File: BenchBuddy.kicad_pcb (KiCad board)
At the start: 4 copper layers, 165.1 x 63.5 mm, 125 parts, among them K1 1461069-5, P1 24 Pin MiniFit JR, P2 CONN_3X2, P3 CONN_2, P4 12 Pin Terminal Block, P5 3 Pin TB, Q1 2N3904, Q2 DMN65D8L-7, Q3 AOD476, Q4 AOD476, SW1 Power Switch, U1 LTV-816S, U11 LM317, U2 MCP3901, U3 LMT84, U4 OPA4170, U5 MCP4801, U6 LM337T, U7 AP5726, U8 LM337T, U9 LM317

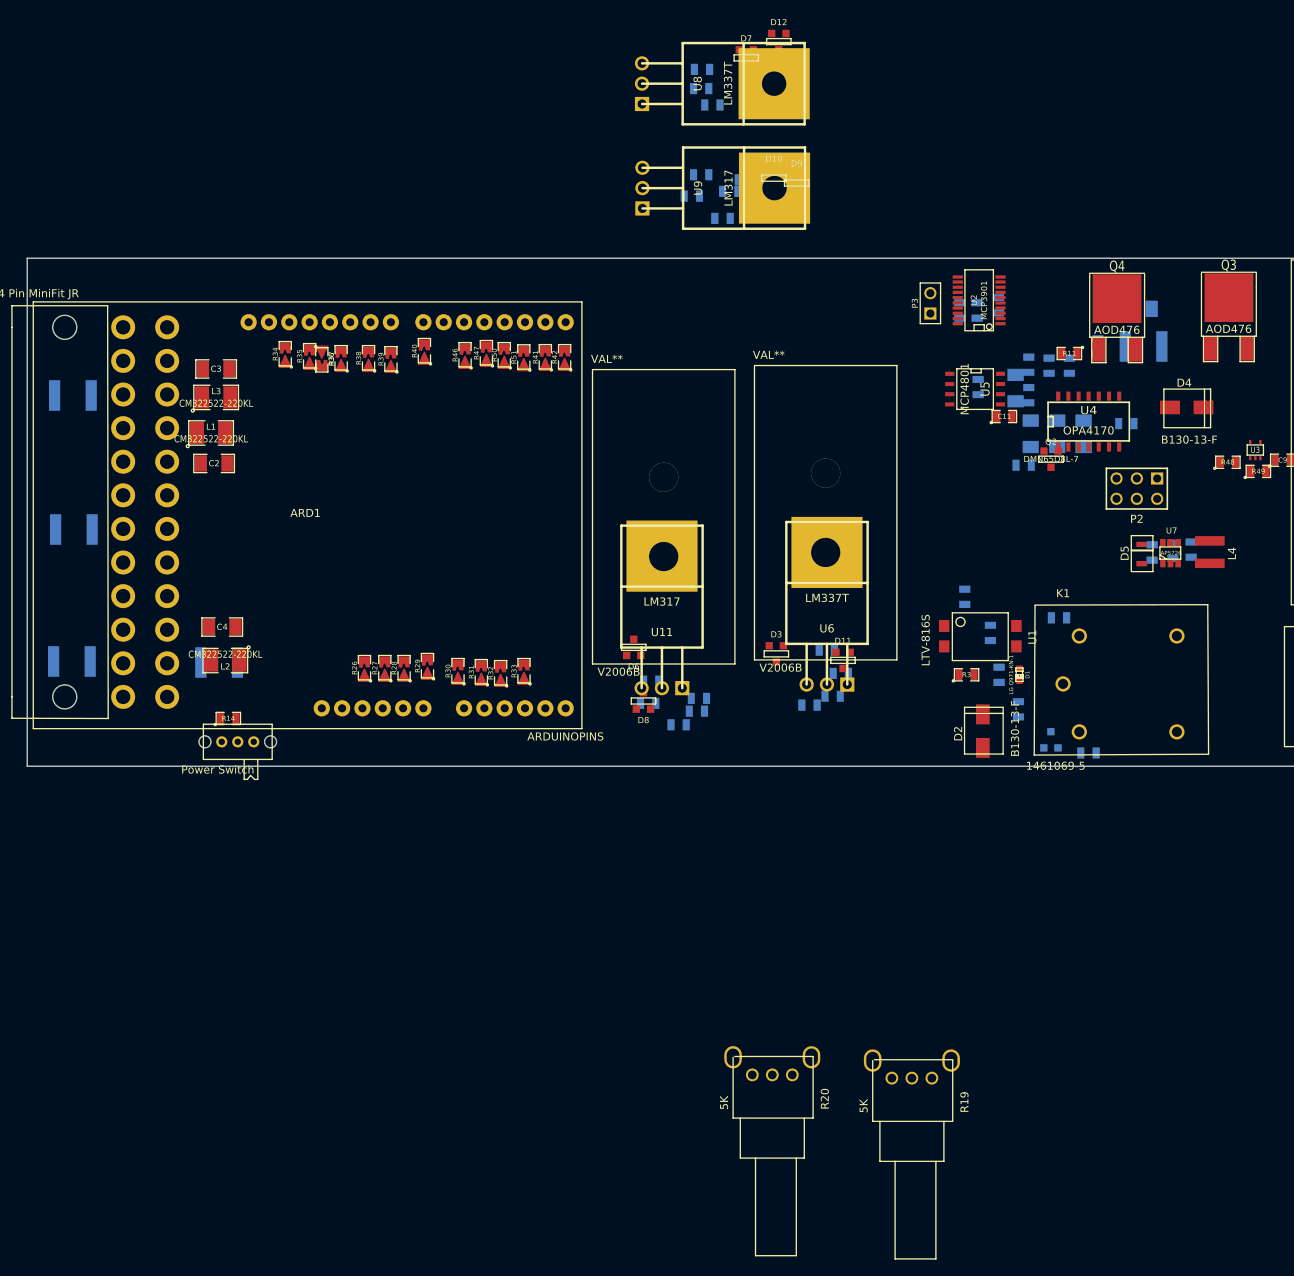
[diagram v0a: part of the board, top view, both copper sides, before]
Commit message: Added more ground planes
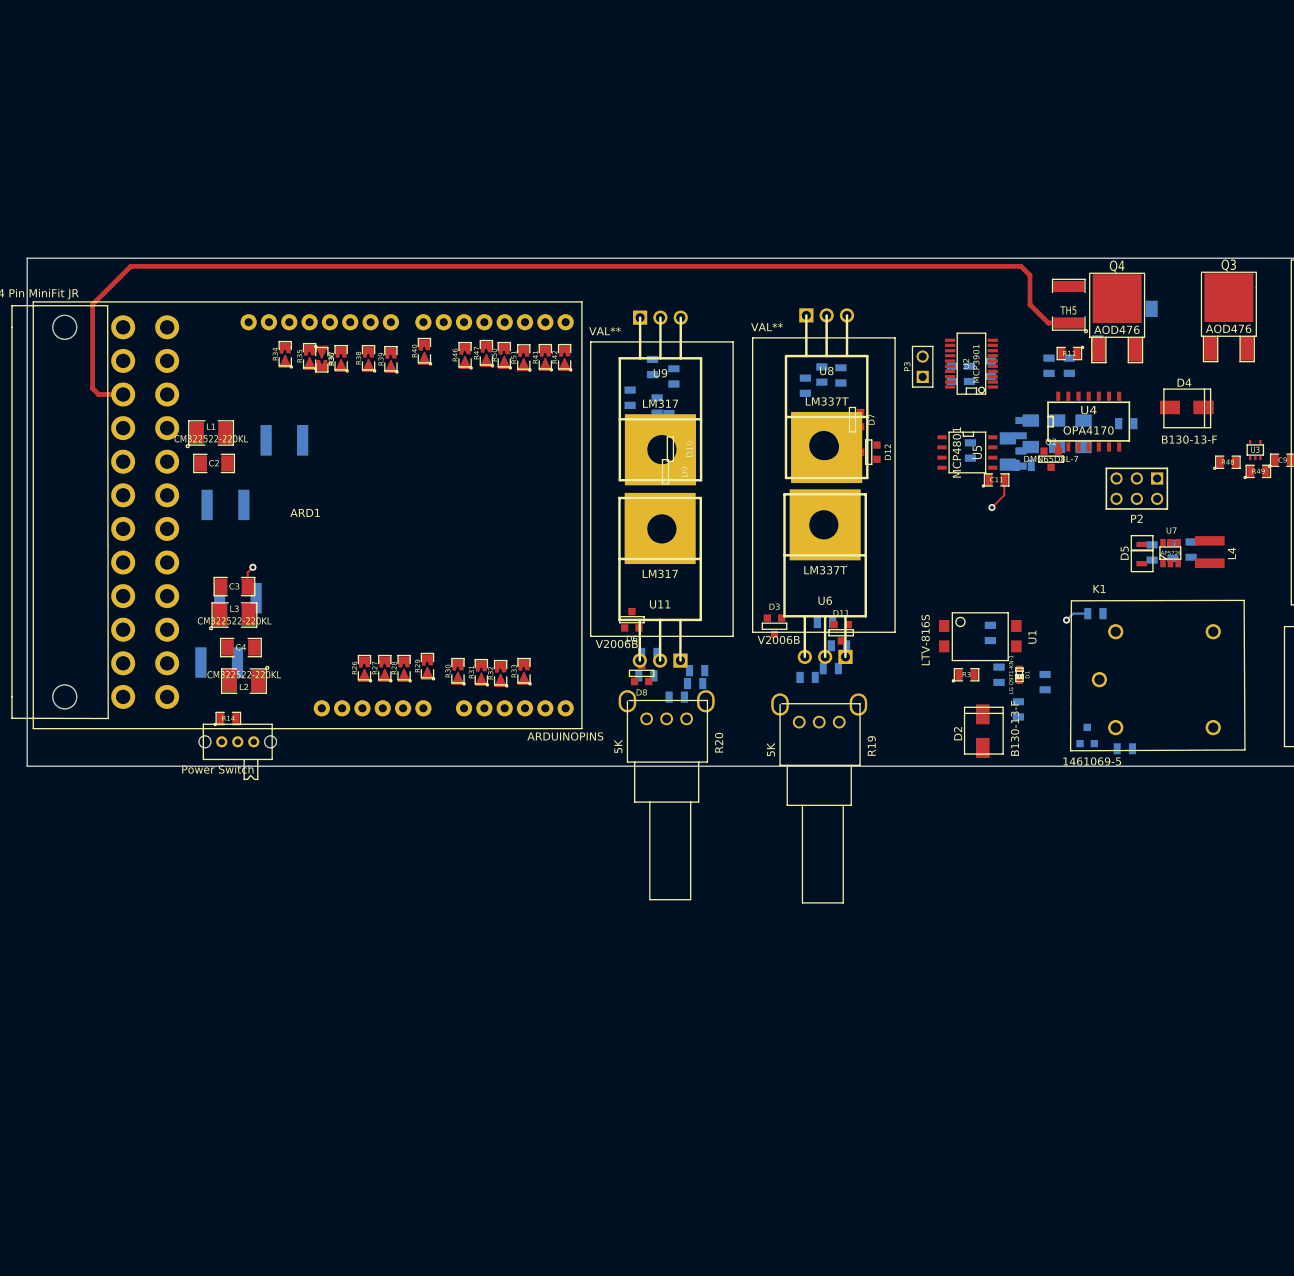
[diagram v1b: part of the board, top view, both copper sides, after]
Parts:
- TH5: moved to F.Cu
- moved D12 52.5 mm to (241.5, 120.0), turned to 270 degrees
- moved C23 50.9 mm to (238.6, 122.0), turned to 90 degrees
- moved C25 48.7 mm to (236.3, 122.3), turned to 270 degrees
- moved D7 47.1 mm to (239.4, 115.9), turned to 270 degrees
- moved R20 46.4 mm to (216.2, 153.3)
- moved R19 46.0 mm to (235.3, 153.7)
- moved R24 45.9 mm to (233.8, 122.2), turned to 270 degrees
- moved R53 42.0 mm to (238.0, 110.4), turned to 270 degrees
- moved C21 40.9 mm to (233.9, 116.4), turned to 270 degrees
- moved D9 39.7 mm to (216.1, 122.5), turned to 270 degrees
- moved C15 38.8 mm to (235.6, 110.3), turned to 270 degrees
- moved U8 37.0 mm to (236.2, 102.9), turned to 270 degrees
- moved R52 37.0 mm to (233.5, 111.7), turned to 270 degrees
- moved D10 36.3 mm to (216.7, 119.6), turned to 270 degrees
- moved R23 35.7 mm to (218.7, 118.1), turned to 270 degrees
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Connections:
- C10 pad 2: -12V -> FE_V-
- C13 pad 2: AGND -> GND
- C9 pad 2: +12V -> FE_V+
- P4 pad 1: +3.3V -> /PowerAdjustmentMonitor/V+_ADJ
- P4 pad 11: /Thermocouple/TC IN + -> /Fan/FAN_OUT-
- P4 pad 12: /Thermocouple/TC IN - -> /Fan/FAN_OUT+
- P4 pad 2: +5V -> /PowerAdjustmentMonitor/V-_ADJ
- P4 pad 4: /PowerAdjustmentMonitor/V+_ADJ -> +3.3V
- P4 pad 5: /PowerAdjustmentMonitor/V-_ADJ -> +5V
- P4 pad 8: /Fan/FAN_OUT+ -> /Thermocouple/TC IN +
- P4 pad 9: /Fan/FAN_OUT- -> /Thermocouple/TC IN -
- Q3 pad 3: AGND -> GND
- R16 pad 2: AGND -> GND
- TH1 pad 2: (no net) -> +3.3V
- U4 pad 11: -12V -> FE_V-
- U4 pad 4: +12V -> FE_V-
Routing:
- net +12C: track 0.00 -> 143.7 mm
- net +3.3V: track 0.00 -> 142.7 mm
- net AGND: track 0.00 -> 4.26 mm, vias 0 -> 1
- net +12P: track 0.00 -> 2.99 mm, vias 0 -> 1
- net +12V: track 0.00 -> 2.69 mm, vias 0 -> 1
- added copper zone on PWR, net +12P
- added copper zone on PWR, net +12V
- added copper zone on PWR, net +3.3V
- added copper zone on PWR, net +5V
- added copper zone on PWR, net -12V
- added copper zone on GND, net AGND
- added copper zone on GND, net GND

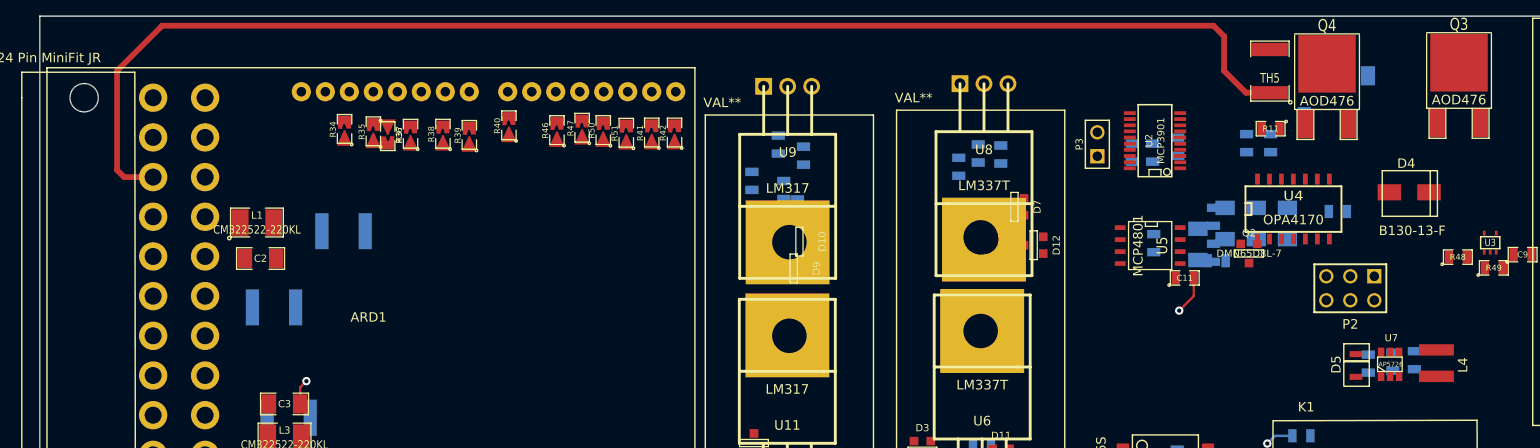
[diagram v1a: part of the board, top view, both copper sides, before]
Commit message: More ground plane changes
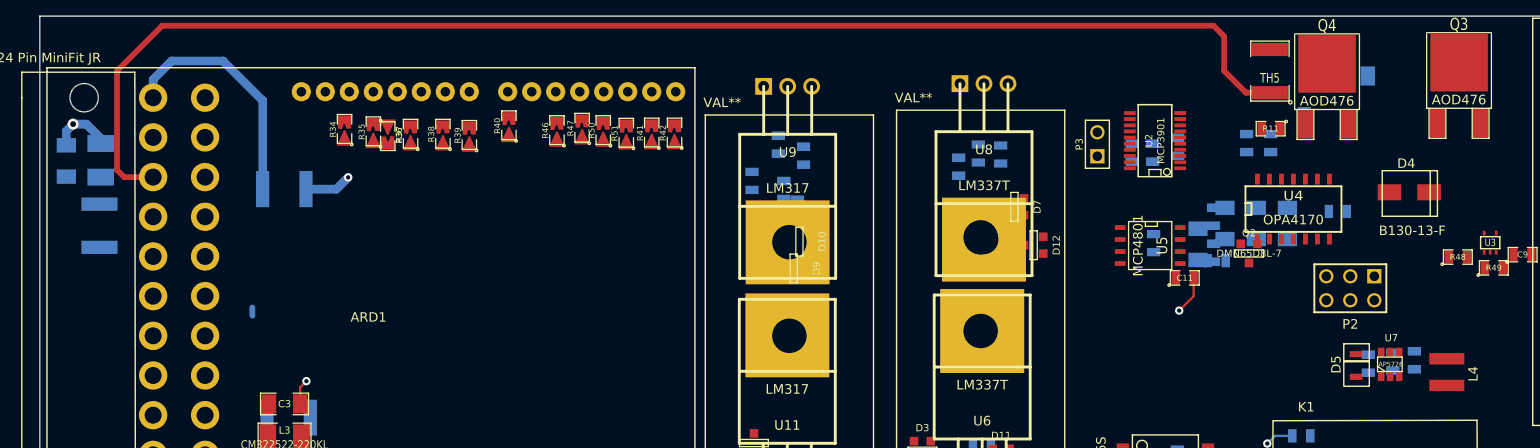
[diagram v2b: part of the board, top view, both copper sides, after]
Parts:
- C2, L1: moved to B.Cu
- moved TH2 25.9 mm to (142.6, 117.9), turned to 90 degrees
- moved C2 23.0 mm to (139.1, 111.1), turned to 270 degrees
- moved L1 17.8 mm to (142.7, 111.0), turned to 90 degrees
- moved TH1 12.6 mm to (162.2, 114.1), turned to 0 degrees
- moved L4 1.44 mm to (285.2, 132.0)
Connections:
- C5 pad 1: +5V -> +5P
- L4 pad 1: +5V -> +5P
- P1 pad 12: (no net) -> N-0000095
- P1 pad 2: N-0000096 (its old number) -> N-0000095
- P4 pad 1: /PowerAdjustmentMonitor/V+_ADJ -> /LED_Driver/LED_STRING+
- P4 pad 2: /PowerAdjustmentMonitor/V-_ADJ -> /LED_Driver/LED_STRING-
- P4 pad 4: +3.3V -> /PowerAdjustmentMonitor/V+_ADJ
- P4 pad 5: +5V -> /PowerAdjustmentMonitor/V-_ADJ
- P4 pad 6: /LED_Driver/LED_STRING+ -> +3.3V
- P4 pad 7: /LED_Driver/LED_STRING- -> +5V
- TH1 pad 1: N-0000096 (its old number) -> N-0000095
- U7 pad 6: +5V -> +5P
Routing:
- net N-0000095: track 0.00 -> 25.4 mm
- net +5V: track 0.00 -> 6.62 mm, vias 0 -> 1
- net +3.3V: track 142.7 -> 140.2 mm, vias 0 -> 1
- net (no net): track 0.00 -> 0.86 mm

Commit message: Cleanup to schematic after doing a scale printout
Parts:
- moved L4 98.7 mm to (188.4, 112.5)
- moved C1 84.4 mm to (174.4, 90.8)
- moved C10 84.4 mm to (191.4, 97.6)
- moved C11 84.4 mm to (175.2, 104.7)
- moved C14 84.4 mm to (132.1, 90.6)
- moved C16 84.4 mm to (154.4, 128.3)
- moved C19 84.4 mm to (131.4, 129.2)
- moved C22 84.4 mm to (137.7, 128.5)
- moved C24 84.4 mm to (134.8, 91.7)
- moved C25 84.4 mm to (154.0, 103.5)
- moved C8 84.4 mm to (171.8, 91.4)
- moved D11 84.4 mm to (155.7, 123.8)
- moved D12 84.4 mm to (159.2, 101.2)
- moved D2 84.4 mm to (173.4, 138.2)
- moved D3 84.4 mm to (147.4, 123.0)
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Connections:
- K1 pad 3: /TerminalBlock/RELAY_NC -> /Relay/RELAY_NC
- K1 pad 4: /Relay/RELAY_NC -> /Relay/RELAY_NO
- P5 pad 1: /Relay/RELAY_NC -> /Relay/RELAY_NO
- P5 pad 3: /TerminalBlock/RELAY_NC -> /Relay/RELAY_NC
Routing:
- net +12C: track 143.7 -> 0.00 mm
- net +3.3V: track 140.2 -> 0.00 mm, vias 1 -> 0
- net N-0000095: track 25.4 -> 0.00 mm
- net +5V: track 6.62 -> 0.00 mm, vias 1 -> 0
- net AGND: track 4.26 -> 0.00 mm, vias 1 -> 0
- net +12P: track 2.99 -> 0.00 mm, vias 1 -> 0
- net +12V: track 2.69 -> 0.00 mm, vias 1 -> 0
- net (no net): track 0.86 -> 0.00 mm
- removed copper zone on PWR, net +12P
- removed copper zone on PWR, net +12V
- removed copper zone on PWR, net +3.3V
- removed copper zone on PWR, net +5V
- removed copper zone on PWR, net -12V
- removed copper zone on GND, net AGND
- removed copper zone on GND, net GND

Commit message: Layout Work Session 1 Output
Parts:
- removed V2006B (x2): VAL**, V2006B
- added 3 mm: VAL**, 3mm-NPTH, F.Cu at (68.9, 80.0)
- added 3 mm: VAL**, 3mm-NPTH, F.Cu at (69.0, 136.9)
- added 3 mm: VAL**, 3mm-NPTH, F.Cu at (207.2, 81.5)
- added JP1: JUMPER, PIN_ARRAY_2X1, F.Cu at (136.0, 64.7)
- U11, U6, U8, U9: footprint TO220 -> TO220_VERT
- moved R20 81.3 mm to (196.1, 82.3), turned to 90 degrees
- moved R21 75.1 mm to (173.9, 64.2)
- moved R22 73.6 mm to (170.3, 64.2)
- moved R25 70.0 mm to (177.6, 64.4)
- moved C19 68.7 mm to (162.4, 67.9)
- moved D8 65.8 mm to (146.8, 65.1)
- moved C17 64.0 mm to (137.0, 67.9)
- moved C22 60.7 mm to (140.6, 67.9)
- moved C16 60.6 mm to (148.0, 68.0)
- moved R19 59.4 mm to (180.9, 82.5), turned to 90 degrees
- moved D3 59.3 mm to (160.0, 65.1)
- moved D11 59.2 mm to (163.2, 65.1)
- moved D6 58.1 mm to (140.3, 65.1)
- moved R18 57.4 mm to (155.2, 68.0)
- moved U11 56.4 mm to (165.5, 81.0)
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
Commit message: Layout Work Session 2 Output
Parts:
- TH5: moved to B.Cu
- moved C11 95.6 mm to (236.1, 99.6)
- moved C14 77.5 mm to (229.4, 60.4)
- moved C15 77.5 mm to (211.3, 60.4)
- moved C20 77.5 mm to (236.7, 60.4)
- moved C21 77.5 mm to (234.8, 60.4)
- moved C23 77.5 mm to (222.3, 60.3)
- moved C24 77.5 mm to (245.8, 60.4)
- moved C25 77.5 mm to (220.3, 60.4)
- moved R52 77.5 mm to (247.6, 60.4)
- moved R53 77.5 mm to (249.4, 60.4)
- moved R54 77.5 mm to (251.2, 60.4)
- moved R55 77.5 mm to (227.6, 60.4)
- moved C17 75.3 mm to (211.2, 55.1)
- moved C19 75.3 mm to (236.6, 55.1)
- moved D10 75.3 mm to (217.7, 52.2)
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
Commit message: Layout Work Session 4 Output
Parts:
- added V8508H: VAL**, V8508H, F.Cu at (160.5, 80.1)
- added V8508H: VAL**, V8508H, F.Cu at (178.2, 79.8)
- moved R19 42.4 mm to (114.2, 80.5)
- moved R20 40.7 mm to (131.1, 80.6)
- moved U11 38.3 mm to (178.4, 86.5)
- moved U6 37.0 mm to (160.4, 86.9)
- moved U2 15.4 mm to (162.9, 98.9), turned to 180 degrees
- moved U8 14.3 mm to (198.2, 86.2)
- moved C12 11.9 mm to (154.6, 117.3)
- moved SW1 8.82 mm to (99.7, 79.2)
- moved P2 8.49 mm to (182.0, 98.8)
- moved U4 5.18 mm to (199.0, 97.6)
- moved U9 2.47 mm to (198.2, 79.5)
- moved D4 2.44 mm to (206.6, 111.0)
- moved Q3 2.44 mm to (198.9, 109.1)
- moved TH5 2.44 mm to (183.1, 108.9)
- moved U5 2.37 mm to (163.1, 109.1), turned to 180 degrees
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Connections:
- C10 pad 1: AGND -> GND_TC
- C11 pad 2: AGND -> GND_TC
- C12 pad 1: AGND -> GND_FAN
- C13 pad 2: GND -> GND_FAN
- C14 pad 2: AGND -> GND_TC
- C15 pad 1: AGND -> GND_TC
- C16 pad 2: AGND -> GND_PWR
- C17 pad 2: AGND -> GND_PWR
- C18 pad 2: AGND -> GND_PWR
- C19 pad 2: AGND -> GND_PWR
- C20 pad 2: AGND -> GND_TC
- C21 pad 1: AGND -> GND_TC
- C22 pad 2: AGND -> GND_PWR
- C23 pad 2: FE_V- -> GND_PWR
- C24 pad 2: AGND -> GND_TC
- C25 pad 2: AGND -> GND_TC
- C5 pad 2: GND -> GND_LED
- C6 pad 2: GND -> GND_LED
- C7 pad 1: AGND -> GND_TC
- C8 pad 2: AGND -> GND_TC
- C9 pad 1: AGND -> GND_TC
- D12 pad 2: AGND -> GND_TC
- P4 pad 10: /Fan/TACH_IN -> +3.3V
- P4 pad 11: /Fan/FAN_OUT- -> /PowerAdjustmentMonitor/V-_ADJ
- P4 pad 12: /Fan/FAN_OUT+ -> /PowerAdjustmentMonitor/V+_ADJ
- P4 pad 3: GND -> /Fan/TACH_IN
- P4 pad 4: /PowerAdjustmentMonitor/V+_ADJ -> /Fan/FAN_OUT-
- P4 pad 5: /PowerAdjustmentMonitor/V-_ADJ -> /Fan/FAN_OUT+
- P4 pad 6: +3.3V -> /Thermocouple/TC IN -
- P4 pad 7: +5V -> /Thermocouple/TC IN +
- P4 pad 8: /Thermocouple/TC IN + -> GND
- P4 pad 9: /Thermocouple/TC IN - -> +5V
- Q2 pad S: AGND -> GND_FAN
- Q3 pad 3: GND -> GND_FAN
- R16 pad 2: GND -> GND_FAN
- R17 pad 2: GND -> GND_LED
- R19 pad 2: AGND -> GND_PWR
- R2 pad 2: GND -> GND_RELAY
- R20 pad 2: AGND -> GND_PWR
- R23 pad 1: AGND -> GND_PWR
- R24 pad 2: AGND -> GND_PWR
- R48 pad 1: AGND -> GND_TC
- R49 pad 1: AGND -> GND_TC
- R52 pad 1: AGND -> GND_TC
- R55 pad 1: AGND -> GND_TC
- R6 pad 2: GND -> GND_RELAY
- R7 pad 1: AGND -> GND_TC
- U2 pad 11: AGND -> GND_TC
- U2 pad 8: AGND -> GND_TC
- U3 pad 1: AGND -> GND_TC
- U3 pad 2: AGND -> GND_TC
- U3 pad 5: AGND -> GND_TC
- U5 pad 7: AGND -> GND_FAN
- U7 pad 2: GND -> GND_LED
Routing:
- net GND_FAN: track 0.00 -> 5.59 mm, vias 0 -> 1
- net GND_TC: track 0.00 -> 4.43 mm, vias 0 -> 1
- net GND_RELAY: track 0.00 -> 3.91 mm, vias 0 -> 1
- net GND_LED: track 0.00 -> 2.83 mm, vias 0 -> 1
- added copper zone on GND, net GND_FAN
- added copper zone on GND, net GND_LED
- added copper zone on GND, net GND_PWR
- added copper zone on GND, net GND_RELAY
- added copper zone on GND, net GND_TC
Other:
- board text added: "Do we need a second GND?"

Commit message: Layout Work Session 5
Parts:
- added TP1: CONN_1, 1pin, F.Cu at (89.7, 113.7)
- moved L2 52.6 mm to (78.8, 83.3)
- moved C4 48.7 mm to (83.3, 81.7), turned to 270 degrees
- moved L3 39.5 mm to (78.9, 88.6)
- moved C3 32.8 mm to (83.6, 90.4), turned to 270 degrees
- moved TH3 19.5 mm to (78.2, 133.6), turned to 0 degrees
- moved U9 11.9 mm to (190.5, 88.5)
- moved P3 11.4 mm to (99.7, 100.8)
- moved TH1 11.0 mm to (68.3, 80.0)
- moved 3 mm 10.3 mm to (58.7, 137.4)
- moved 3 mm 9.99 mm to (58.9, 79.8)
- moved Q3 8.66 mm to (207.5, 109.0)
- moved D4 8.48 mm to (207.5, 102.6)
- moved L1 7.84 mm to (52.6, 92.2)
- moved TH2 7.46 mm to (52.8, 99.3)
- moved Q4 5.45 mm to (188.0, 109.2)
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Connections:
- C10 pad 1: GND_TC -> AGND
- C11 pad 2: GND_TC -> AGND
- C12 pad 1: GND_FAN -> AGND
- C13 pad 2: GND_FAN -> AGND
- C14 pad 2: GND_TC -> AGND
- C15 pad 1: GND_TC -> AGND
- C20 pad 2: GND_TC -> AGND
- C21 pad 1: GND_TC -> AGND
- C24 pad 2: GND_TC -> AGND
- C25 pad 2: GND_TC -> AGND
- C7 pad 1: GND_TC -> AGND
- C8 pad 2: GND_TC -> AGND
- C9 pad 1: GND_TC -> AGND
- D12 pad 2: GND_TC -> AGND
- P4 pad 8: GND -> GND_PWR
- Q2 pad S: GND_FAN -> AGND
- Q3 pad 3: GND_FAN -> AGND
- R16 pad 2: GND_FAN -> AGND
- R48 pad 1: GND_TC -> AGND
- R49 pad 1: GND_TC -> AGND
- R52 pad 1: GND_TC -> AGND
- R55 pad 1: GND_TC -> AGND
- R7 pad 1: GND_TC -> AGND
- U2 pad 11: GND_TC -> AGND
- U2 pad 8: GND_TC -> AGND
- U3 pad 1: GND_TC -> AGND
- U3 pad 2: GND_TC -> AGND
- U3 pad 5: GND_TC -> AGND
- U5 pad 7: GND_FAN -> AGND
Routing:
- net +12V: track 0.00 -> 203.4 mm, vias 0 -> 1
- net -12V: track 0.00 -> 199.9 mm, vias 0 -> 1
- net +12C: track 0.00 -> 187.2 mm, vias 0 -> 2
- net /Relay/RELAY_COM: track 0.00 -> 24.0 mm
- net /Relay/RELAY_NO: track 0.00 -> 10.2 mm
- net /Relay/RELAY_NC: track 0.00 -> 9.62 mm
- net GND_FAN: track 5.59 -> 0.00 mm, vias 1 -> 0
- net GND_TC: track 4.43 -> 0.00 mm, vias 1 -> 0
- net +5P: track 0.00 -> 2.70 mm, vias 0 -> 1
- net +12P: track 0.00 -> 2.27 mm, vias 0 -> 1
- net GND_RELAY: track 3.91 -> 1.65 mm
- net AGND: track 0.00 -> 1.91 mm, vias 0 -> 1
- net +5V: track 0.00 -> 1.78 mm, vias 0 -> 1
- added copper zone on PWR, net +12P
- added copper zone on PWR, net +5P
- added copper zone on PWR, net +5V
- added copper zone on GND, net AGND
- removed copper zone on GND, net GND_FAN
- removed copper zone on GND, net GND_TC
